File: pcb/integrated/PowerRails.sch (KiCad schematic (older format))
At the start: 33 parts, among them U9001 EC6AW, U9002 RAC10, U9003 TPS82140, U9004 TPS82140, U9005 TPS735, U9006 TPS735

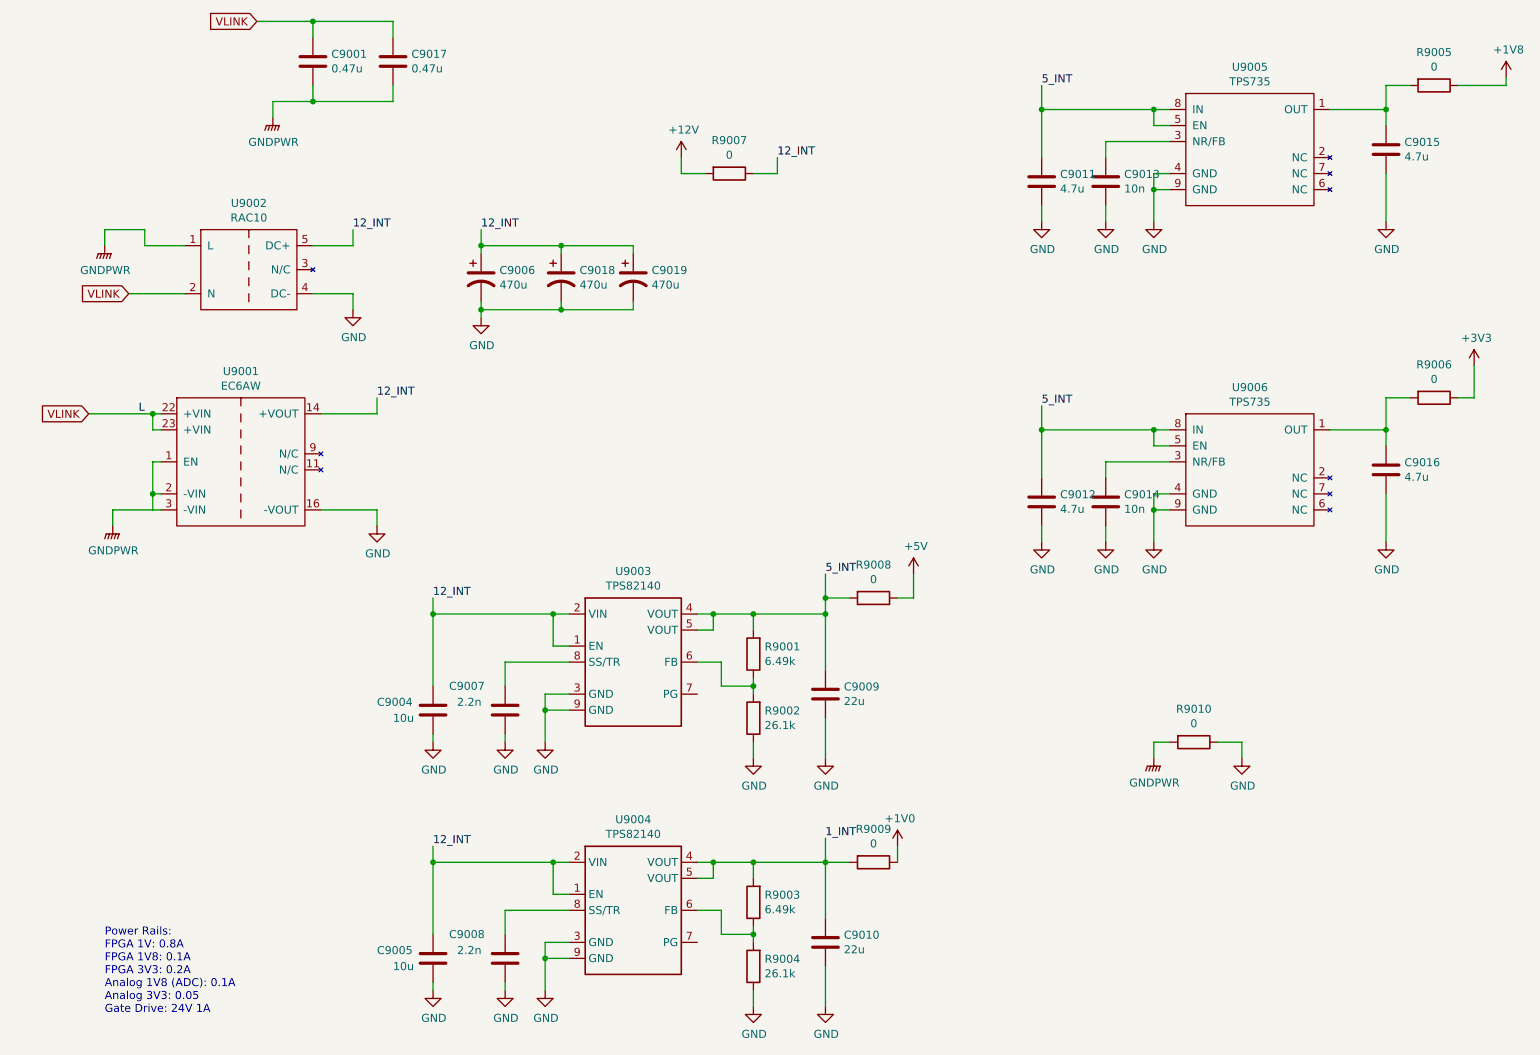
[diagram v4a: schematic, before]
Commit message: updated component values for schematic
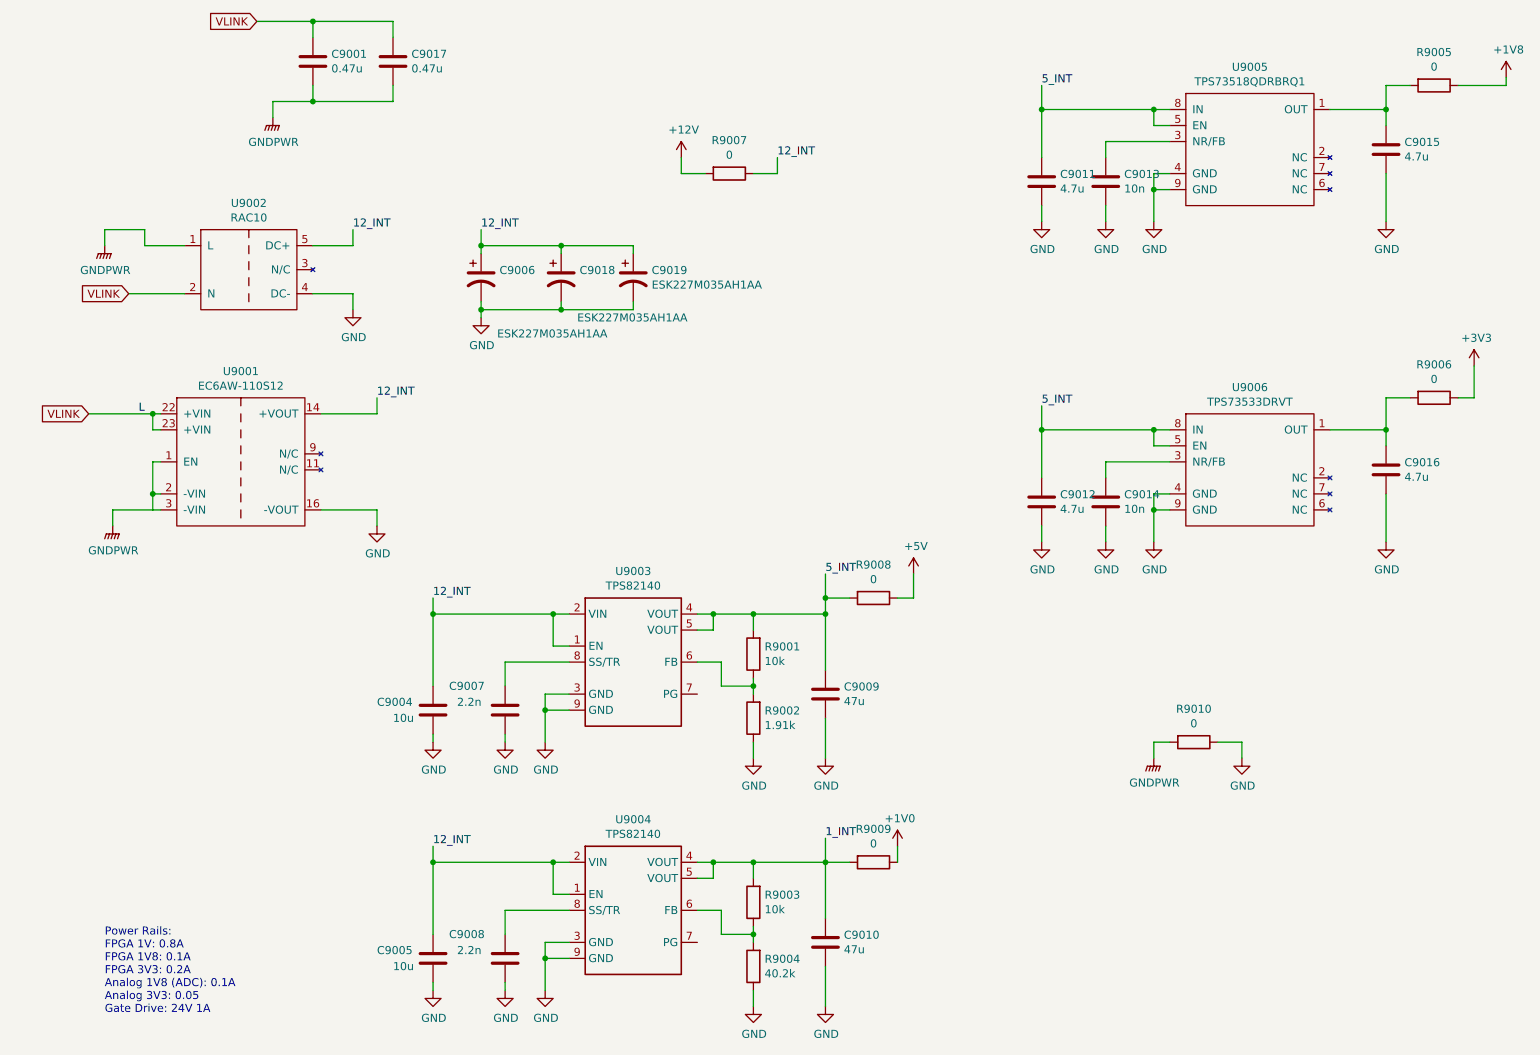
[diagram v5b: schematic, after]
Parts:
- C9006, C9018, C9019: value 470u -> ESK227M035AH1AA
- C9009, C9010: value 22u -> 47u
- R9001, R9003: value 6.49k -> 10k
- R9002: value 26.1k -> 1.91k
- R9004: value 26.1k -> 40.2k
- U9001: value EC6AW -> EC6AW-110S12
- U9005: value TPS735 -> TPS73518QDRBRQ1
- U9006: value TPS735 -> TPS73533DRVT
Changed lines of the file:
@@
 EESchema Schematic File Version 4
 LIBS:integrated-cache
-EELAYER 30 0
+EELAYER 26 0
 EELAYER END
 $Descr A4 11693 8268
@@
 P 4200 2600
 F 0 "C9006" H 4315 2646 50  0000 L CNN
-F 1 "470u" H 4315 2555 50  0000 L CNN
+F 1 "ESK227M035AH1AA" H 4300 2250 50  0000 L CNN
 F 2 "Capacitor_THT:CP_Radial_D10.0mm_P5.00mm" H 4200 2600 50  0001 C CNN
 F 3 "~" H 4200 2600 50  0001 C CNN
@@
 P 9000 1800
 F 0 "U9005" H 9000 2315 50  0000 C CNN
-F 1 "TPS735" H 9000 2224 50  0000 C CNN
+F 1 "TPS73518QDRBRQ1" H 9000 2224 50  0000 C CNN
 F 2 "wbraun_smd:SON-8_EP" H 9700 1550 50  0001 C CNN
 F 3 "" H 9700 1550 50  0001 C CNN
@@
 P 9000 3800
 F 0 "U9006" H 9000 4315 50  0000 C CNN
-F 1 "TPS735" H 9000 4224 50  0000 C CNN
+F 1 "TPS73533DRVT" H 9000 4224 50  0000 C CNN
 F 2 "wbraun_smd:SON-8_EP" H 9700 3550 50  0001 C CNN
 F 3 "" H 9700 3550 50  0001 C CNN
@@
 P 5900 4950
 F 0 "R9001" H 5830 4904 50  0000 R CNN
-F 1 "6.49k" H 5830 4995 50  0000 R CNN
+F 1 "10k" H 5830 4995 50  0000 R CNN
 F 2 "Resistor_SMD:R_0402_1005Metric" V 5830 4950 50  0001 C CNN
 F 3 "~" H 5900 4950 50  0001 C CNN
@@
 P 5900 5350
 F 0 "R9002" H 5830 5304 50  0000 R CNN
-F 1 "26.1k" H 5830 5395 50  0000 R CNN
+F 1 "1.91k" H 5830 5395 50  0000 R CNN
 F 2 "Resistor_SMD:R_0402_1005Metric" V 5830 5350 50  0001 C CNN
 F 3 "~" H 5900 5350 50  0001 C CNN
@@
 P 6350 5200
 F 0 "C9009" H 6465 5246 50  0000 L CNN
-F 1 "22u" H 6465 5155 50  0000 L CNN
+F 1 "47u" H 6465 5155 50  0000 L CNN
 F 2 "Capacitor_SMD:C_0805_2012Metric" H 6388 5050 50  0001 C CNN
 F 3 "~" H 6350 5200 50  0001 C CNN
@@
 P 2700 3750
 F 0 "U9001" H 2700 4315 50  0000 C CNN
-F 1 "EC6AW" H 2700 4224 50  0000 C CNN
+F 1 "EC6AW-110S12" H 2700 4224 50  0000 C CNN
 F 2 "wbraun_smd:EC6AW" H 2800 3200 50  0001 C CNN
 F 3 "" H 2800 3200 50  0001 C CNN
@@
 P 5900 6500
 F 0 "R9003" H 5830 6454 50  0000 R CNN
-F 1 "6.49k" H 5830 6545 50  0000 R CNN
+F 1 "10k" H 5830 6545 50  0000 R CNN
 F 2 "Resistor_SMD:R_0402_1005Metric" V 5830 6500 50  0001 C CNN
 F 3 "~" H 5900 6500 50  0001 C CNN
@@
 P 5900 6900
 F 0 "R9004" H 5830 6854 50  0000 R CNN
-F 1 "26.1k" H 5830 6945 50  0000 R CNN
+F 1 "40.2k" H 5830 6945 50  0000 R CNN
 F 2 "Resistor_SMD:R_0402_1005Metric" V 5830 6900 50  0001 C CNN
 F 3 "~" H 5900 6900 50  0001 C CNN
@@
 P 6350 6750
 F 0 "C9010" H 6465 6796 50  0000 L CNN
-F 1 "22u" H 6465 6705 50  0000 L CNN
+F 1 "47u" H 6465 6705 50  0000 L CNN
 F 2 "Capacitor_SMD:C_0805_2012Metric" H 6388 6600 50  0001 C CNN
 F 3 "~" H 6350 6750 50  0001 C CNN
@@
 P 4700 2600
 F 0 "C9018" H 4815 2646 50  0000 L CNN
-F 1 "470u" H 4815 2555 50  0000 L CNN
+F 1 "ESK227M035AH1AA" H 4800 2350 50  0000 L CNN
 F 2 "Capacitor_THT:CP_Radial_D10.0mm_P5.00mm" H 4700 2600 50  0001 C CNN
 F 3 "~" H 4700 2600 50  0001 C CNN
@@
 P 5150 2600
 F 0 "C9019" H 5265 2646 50  0000 L CNN
-F 1 "470u" H 5265 2555 50  0000 L CNN
+F 1 "ESK227M035AH1AA" H 5265 2555 50  0000 L CNN
 F 2 "Capacitor_THT:CP_Radial_D10.0mm_P5.00mm" H 5150 2600 50  0001 C CNN
 F 3 "~" H 5150 2600 50  0001 C CNN
